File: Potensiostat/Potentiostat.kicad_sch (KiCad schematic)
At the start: 0 parts

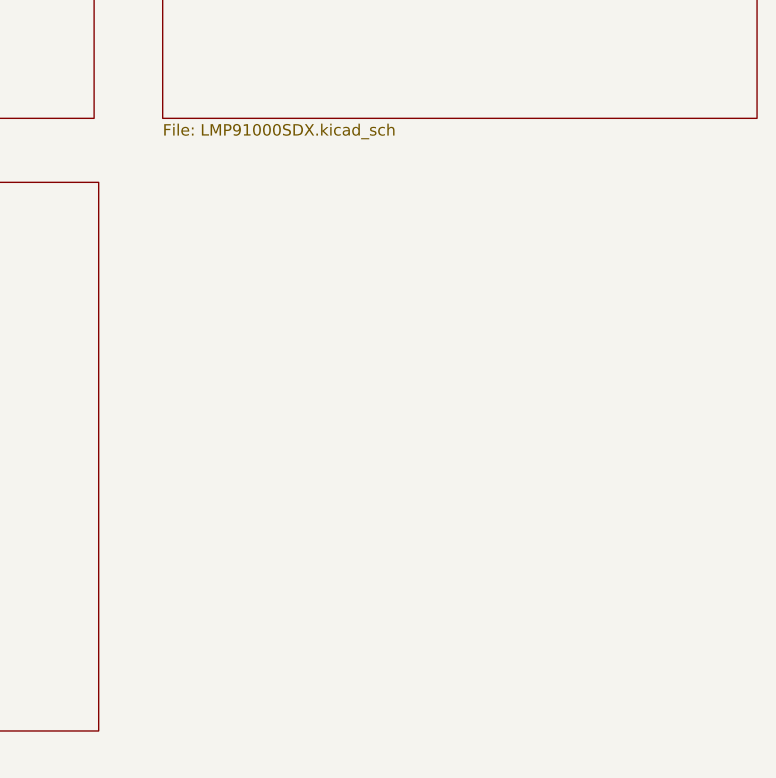
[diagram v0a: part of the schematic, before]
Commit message: Added LMP USP-UART
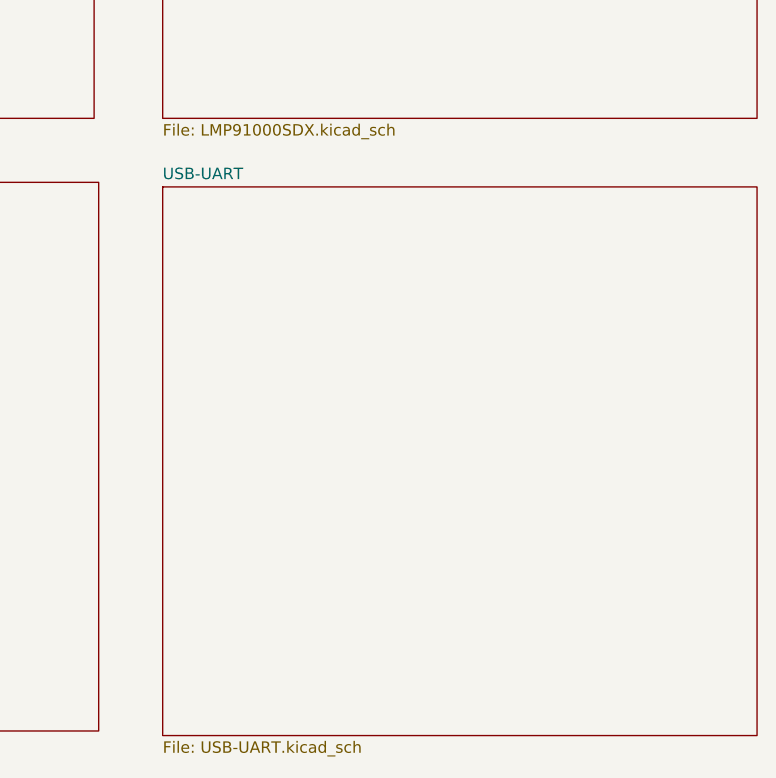
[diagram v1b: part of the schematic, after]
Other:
- added sheet USB-UART (USB-UART.kicad_sch)
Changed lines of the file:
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@@
+	)
+	(sheet
+		(at 91.44 87.63)
+		(size 66.04 60.96)
+		(exclude_from_sim no)
+		(in_bom yes)
+		(on_board yes)
+		(dnp no)
+		(fields_autoplaced yes)
+		(stroke
+			(width 0.1524)
+			(type solid)
+		)
+		(fill
+			(color 0 0 0 0.0000)
+		)
+		(property "Sheetname" "USB-UART"
+			(at 91.44 86.9184 0)
+			(effects
+				(font
+					(size 1.27 1.27)
+				)
+				(justify left bottom)
+			)
+		)
+		(property "Sheetfile" "USB-UART.kicad_sch"
+			(at 91.44 149.1746 0)
+			(effects
+				(font
+					(size 1.27 1.27)
+				)
+				(justify left top)
+			)
+		)
+		(instances
+			(project "Potentiostat"
+				(path "/be108998-ac86-4f7d-931a-841db1905f2a"
+					(page "5")
+				)
+			)
+		)
 	)
 	(sheet
